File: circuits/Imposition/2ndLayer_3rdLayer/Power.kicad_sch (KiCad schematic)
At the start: 68 parts, among them Q1 SSM3J332R, Q10 S8550, Q11 SSM3J332R, Q12 S8550, Q17 SSM3J332R, Q18 2N7002, Q2 S8550, Q3 SSM3J332R, Q4 S8550, Q7 SSM6J808R, Q8 2N7002, Q9 SSM6J808R, SW2 SW_SPDT_White, U1 DCDC_TPSM336x5, U7 AZ1117CH-3.3

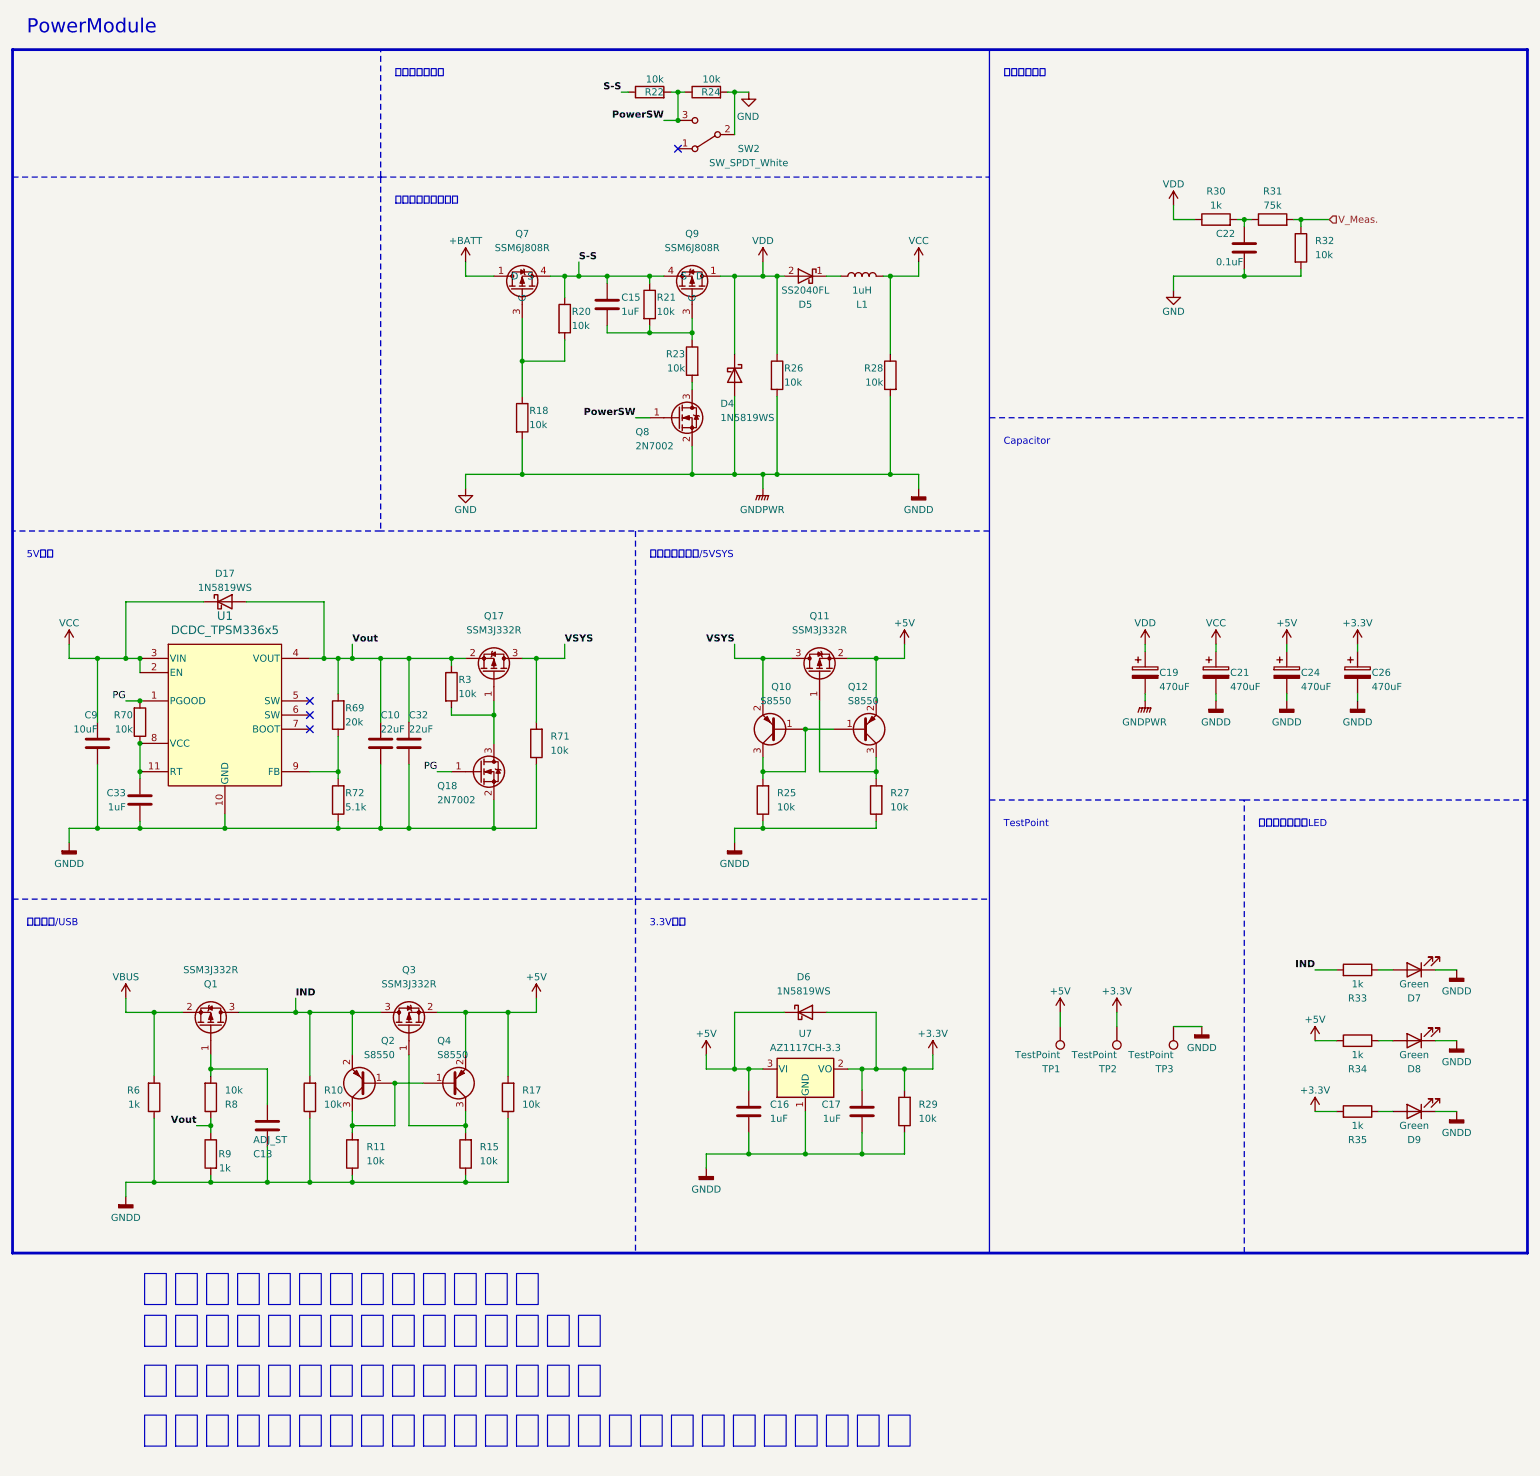
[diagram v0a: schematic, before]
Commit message: 発注_第一弾
Drive, 1stLayer_Power, 2ndLayer_3rdLayer
を発注
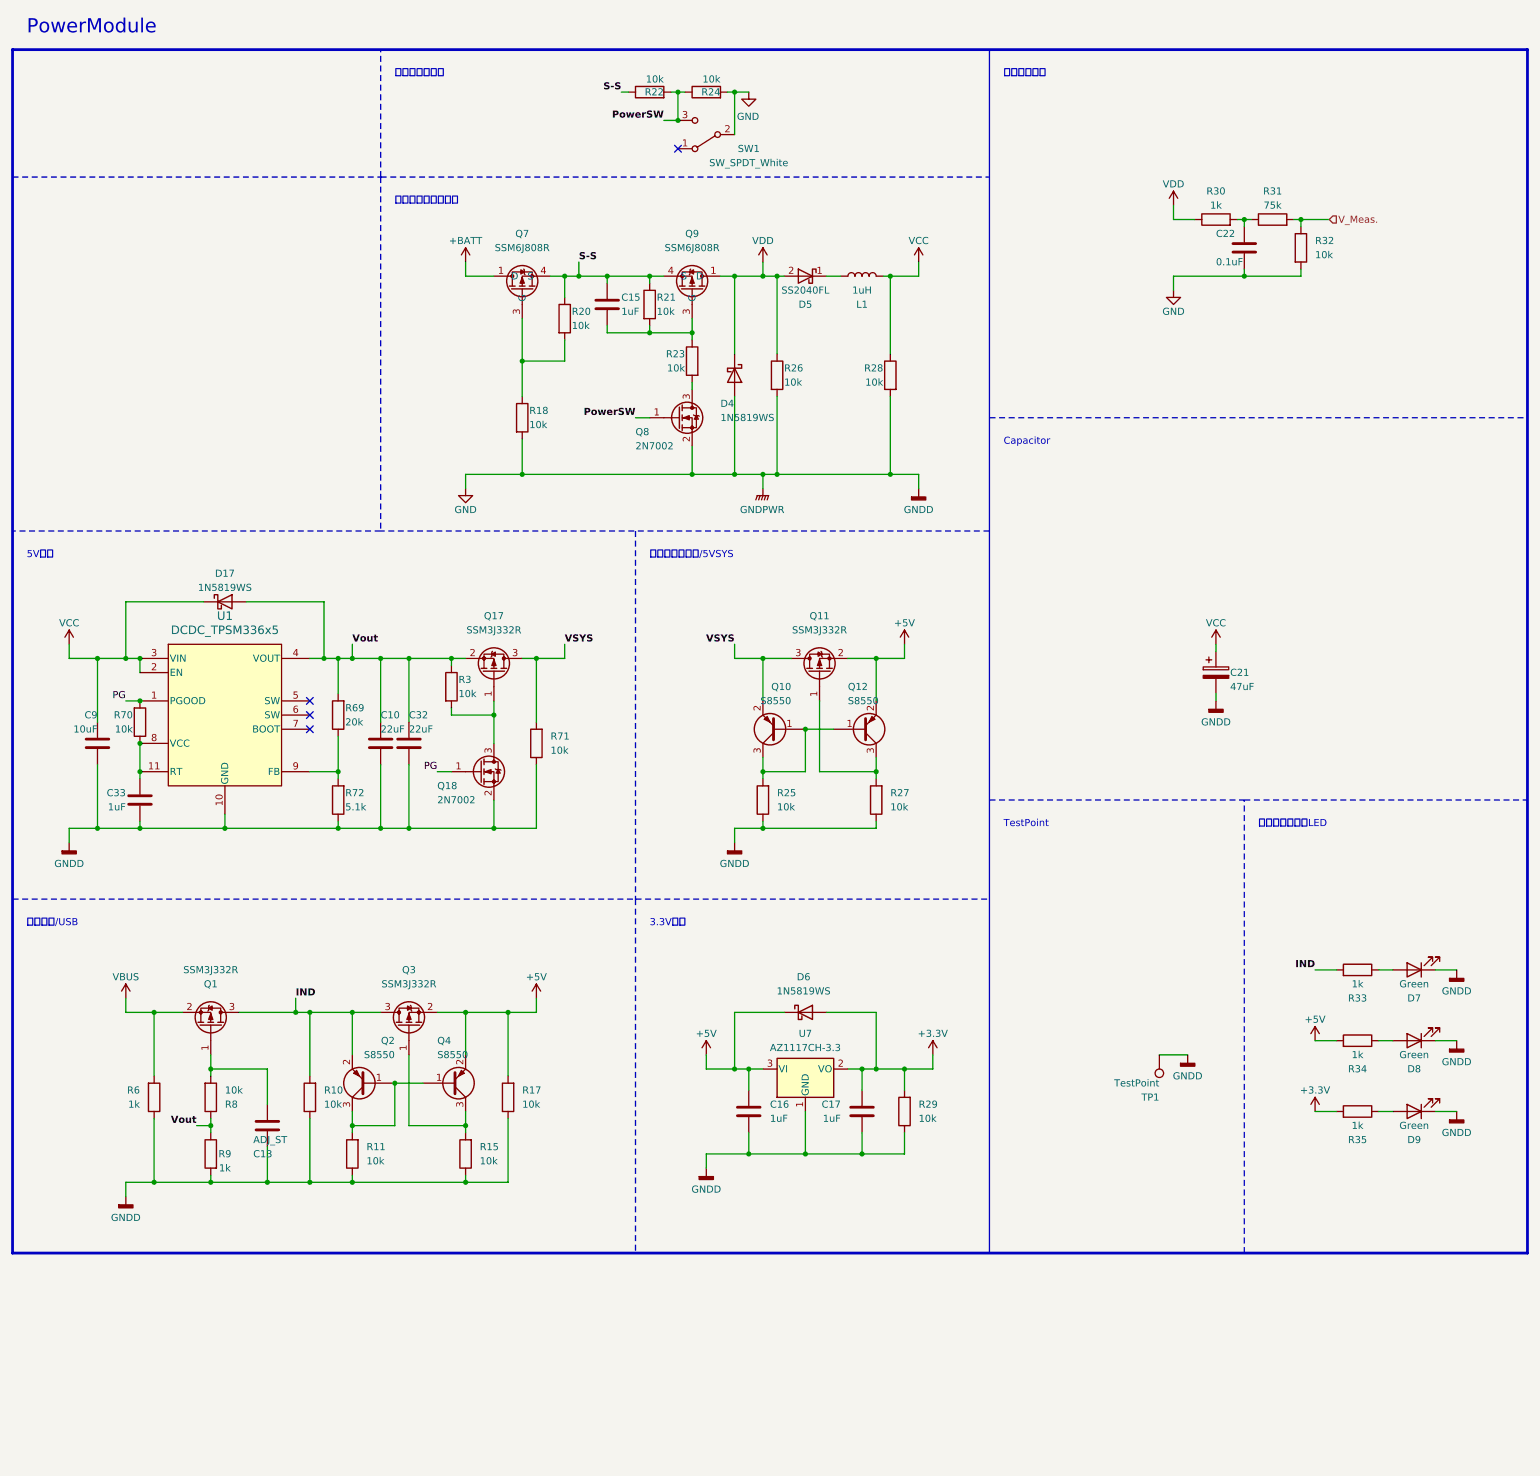
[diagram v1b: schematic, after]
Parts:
- removed C19, C24, C26: 470uF, symbol Device:C_Polarized
- removed TP2, TP3: TestPoint, TestPoint:TestPoint_THTPad_D2.0mm_Drill1.0mm, symbol Connector:TestPoint
- C21: value 470uF -> 47uF; footprint (none) -> Capacitor_SMD:CP_Elec_6.3x5.4
- renumbered SW2 to SW1
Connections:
- net +5V: no longer TP1.1
- net GND: now also TP1.1
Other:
- note removed: "三端子を新しく選定したのにする 電源直付けのための穴を設定する 電源平滑コンデンサは基板設計の時に良い感じに数調整"
- note removed: "電源スイッチ 耐圧大丈夫？"

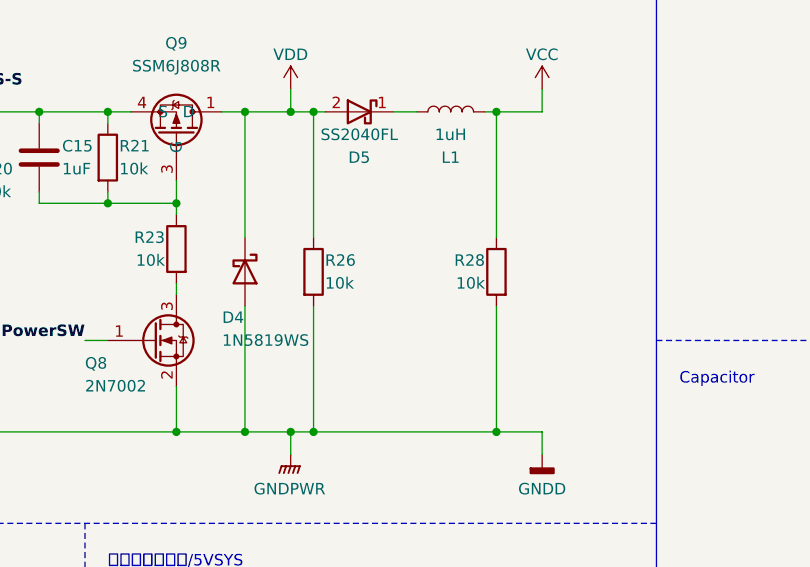
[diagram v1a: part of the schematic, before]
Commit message: 発注第2弾
RasPi発注
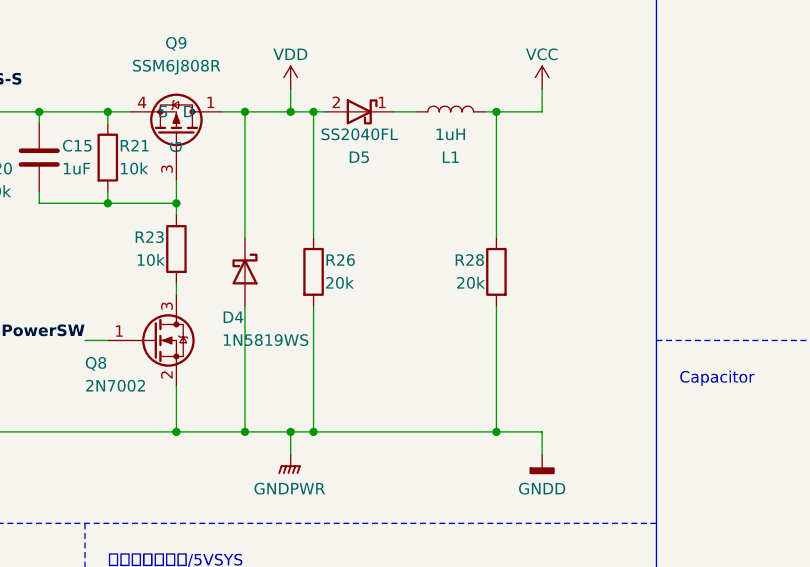
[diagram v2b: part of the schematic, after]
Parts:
- R26, R28: value 10k -> 20k
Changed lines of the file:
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@@
       (effects (font (size 1.27 1.27)) (justify left))
     )
-    (property "Value" "10k" (at 232.41 90.17 0)
+    (property "Value" "20k" (at 232.41 90.17 0)
       (effects (font (size 1.27 1.27)) (justify left))
     )
@@
       (effects (font (size 1.27 1.27)) (justify left))
     )
-    (property "Value" "10k" (at 250.19 90.17 0)
-      (effects (font (size 1.27 1.27)) (justify left))
-    )
+    (property "Value" "20k" (at 250.19 90.17 0)
+      (effects (font (size 1.27 1.27)) (justify left))
+    )
